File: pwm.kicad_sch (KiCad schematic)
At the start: 10 parts, among them U501 LTC6992IS6-1

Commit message: update datasheets and footprint references
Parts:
- C401: footprint pss:C_0805_2012Metric_Pad1.18x1.45mm_HandSolder -> enclosure:C_0805_2012Metric_Pad1.18x1.45mm_HandSolder
- R401, R402, R403, R404, R405: footprint pss:R_1210_3225Metric_Pad1.30x2.65mm_HandSolder -> enclosure:R_1210_3225Metric_Pad1.30x2.65mm_HandSolder
- TP401, TP402, TP403: footprint pss:TP_0805_2012Metric -> enclosure:TP_0805_2012Metric
- U501: footprint Package_TO_SOT_SMD:TSOT-23-6 -> enclosure:TSOT-23-6
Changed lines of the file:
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@@
 			)
 		)
-		(property "Footprint" "pss:TP_0805_2012Metric"
+		(property "Footprint" "enclosure:TP_0805_2012Metric"
 			(at 96.52 101.6 0)
 			(effects
@@
 			)
 		)
-		(property "Footprint" "pss:R_1210_3225Metric_Pad1.30x2.65mm_HandSolder"
+		(property "Footprint" "enclosure:R_1210_3225Metric_Pad1.30x2.65mm_HandSolder"
 			(at 116.078 109.22 90)
 			(effects
@@
 			)
 		)
-		(property "Footprint" "pss:R_1210_3225Metric_Pad1.30x2.65mm_HandSolder"
+		(property "Footprint" "enclosure:R_1210_3225Metric_Pad1.30x2.65mm_HandSolder"
 			(at 90.678 109.22 90)
 			(effects
@@
 			)
 		)
-		(property "Footprint" "pss:R_1210_3225Metric_Pad1.30x2.65mm_HandSolder"
+		(property "Footprint" "enclosure:R_1210_3225Metric_Pad1.30x2.65mm_HandSolder"
 			(at 90.678 93.98 90)
 			(effects
@@
 			)
 		)
-		(property "Footprint" "pss:C_0805_2012Metric_Pad1.18x1.45mm_HandSolder"
+		(property "Footprint" "enclosure:C_0805_2012Metric_Pad1.18x1.45mm_HandSolder"
 			(at 164.1348 81.28 0)
 			(effects
@@
 			)
 		)
-		(property "Footprint" "pss:R_1210_3225Metric_Pad1.30x2.65mm_HandSolder"
+		(property "Footprint" "enclosure:R_1210_3225Metric_Pad1.30x2.65mm_HandSolder"
 			(at 116.078 93.98 90)
 			(effects
@@
 			)
 		)
-		(property "Footprint" "pss:R_1210_3225Metric_Pad1.30x2.65mm_HandSolder"
+		(property "Footprint" "enclosure:R_1210_3225Metric_Pad1.30x2.65mm_HandSolder"
 			(at 141.478 109.22 90)
 			(effects
@@
 			)
 		)
-		(property "Footprint" "pss:TP_0805_2012Metric"
+		(property "Footprint" "enclosure:TP_0805_2012Metric"
 			(at 182.88 101.6 0)
 			(effects
@@
 			)
 		)
-		(property "Footprint" "pss:TP_0805_2012Metric"
+		(property "Footprint" "enclosure:TP_0805_2012Metric"
 			(at 123.19 99.06 0)
 			(effects
@@
 			)
 		)
-		(property "Footprint" "Package_TO_SOT_SMD:TSOT-23-6"
+		(property "Footprint" "enclosure:TSOT-23-6"
 			(at 152.4 111.76 0)
 			(effects

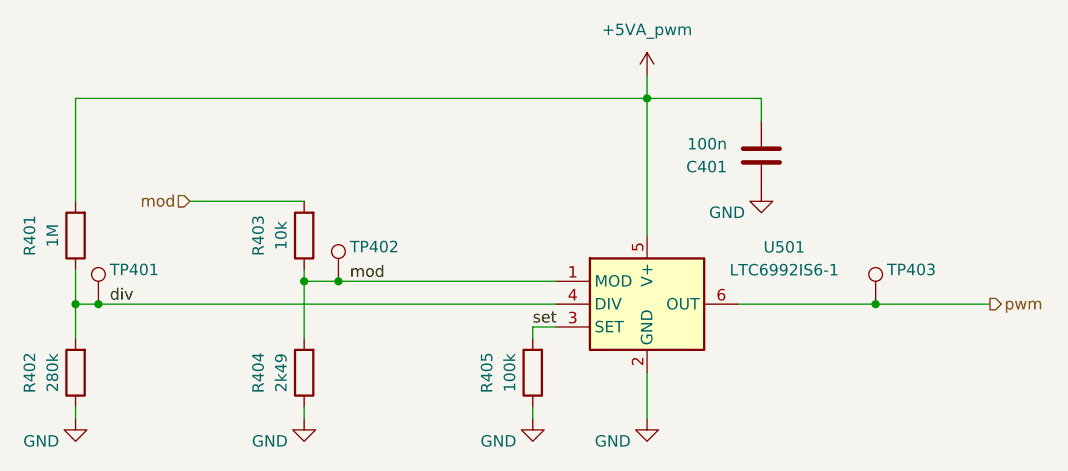
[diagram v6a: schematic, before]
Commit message: add pwm sub layout
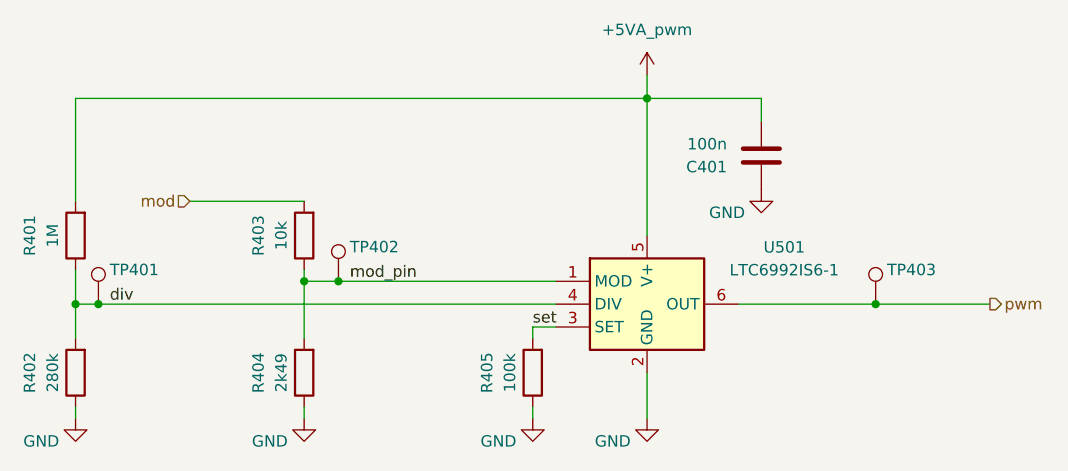
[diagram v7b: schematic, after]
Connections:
- net mod: no longer R403.1, R404.2, TP402.1, U501.1 (MOD)
- new net mod_pin: R403.1, R404.2, TP402.1, U501.1 (MOD)
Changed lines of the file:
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@@
 		)
 	)
-	(label "mod"
+	(label "mod_pin"
 		(at 119.38 99.06 0)
 		(fields_autoplaced yes)
